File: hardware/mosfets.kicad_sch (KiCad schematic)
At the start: 11 parts, among them Q21 AO3400A, Q22 AO3400A

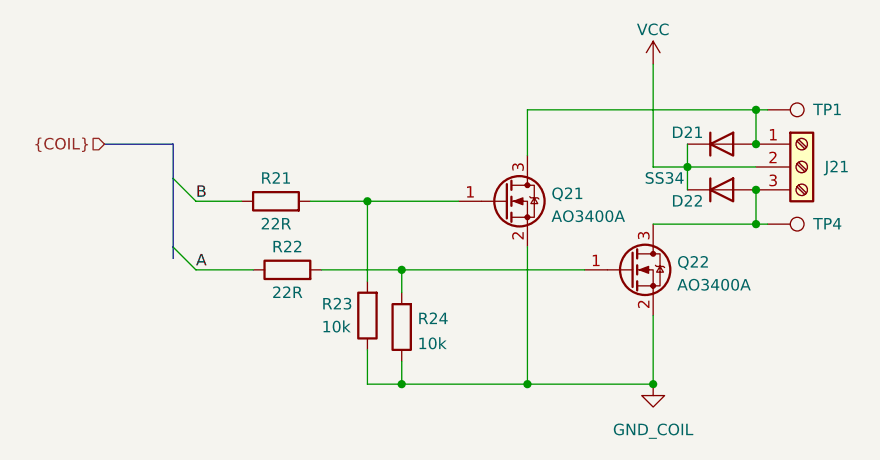
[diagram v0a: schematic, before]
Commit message: organized board files and added pictures
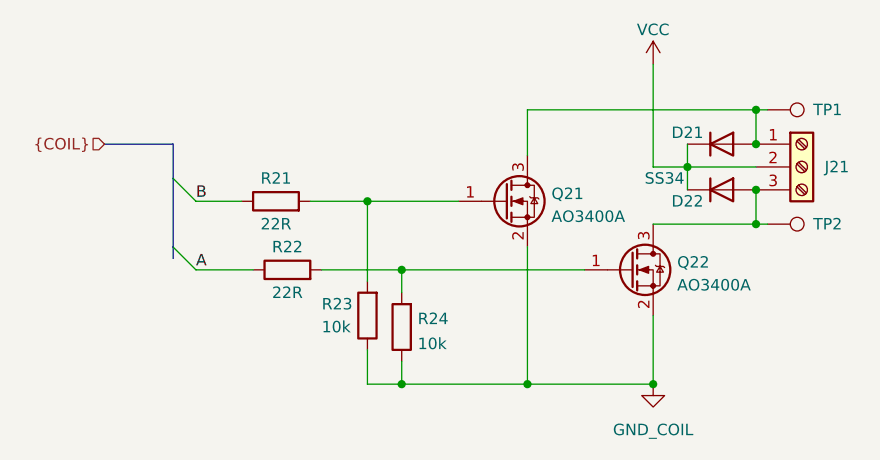
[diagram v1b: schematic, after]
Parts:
- renumbered TP4 to TP2
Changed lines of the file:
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@@
 		(on_board yes)
 		(dnp no)
-		(property "Reference" "TP4"
+		(property "Reference" "TP2"
 			(at 167.64 40.64 90)
 			(effects
@@
 		(on_board yes)
 		(dnp no)
-		(property "Reference" "#PWR01201"
+		(property "Reference" "#PWR0401"
 			(at 149.86 26.67 0)
 			(effects
@@
 		(dnp no)
 		(fields_autoplaced yes)
-		(property "Reference" "#PWR0602"
+		(property "Reference" "#PWR0402"
 			(at 149.86 64.77 0)
 			(effects
